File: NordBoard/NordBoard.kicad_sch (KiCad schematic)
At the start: 0 parts

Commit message: feat: readme & begin project
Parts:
- added SW1: SW_Push, symbol Switch:SW_Push
- added U1: MOUDLE-SEEEDUINO-XIAO, symbol XIAO_RP2040:MOUDLE-SEEEDUINO-XIAO
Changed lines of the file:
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@@
 	(generator_version "9.0")
 	(paper "A4")
+	(symbol
+		(lib_id "XIAO_RP2040:MOUDLE-SEEEDUINO-XIAO")
+		(at 58.42 48.26 0)
+		(unit 1)
+		(exclude_from_sim no)
+		(in_bom yes)
+		(on_board yes)
+		(dnp no)
+		(fields_autoplaced yes)
+		(property "Reference" "U1"
+			(at 59.69 33.02 0)
+			(effects
+				(font
+					(size 1.27 1.27)
+				)
+			)
+		)
+		(property "Value" "MOUDLE-SEEEDUINO-XIAO"
+			(at 59.69 35.56 0)
+			(effects
+				(font
+					(size 1.27 1.27)
+				)
+			)
+		)
+		(property "Footprint" ""
+			(at 41.91 45.72 0)
+			(effects
+				(font
+					(size 1.27 1.27)
+				)
+				(hide yes)
+			)
+		)
+		(property "Datasheet" ""
+			(at 41.91 45.72 0)
+			(effects
+				(font
+					(size 1.27 1.27)
+				)
+				(hide yes)
+			)
+		)
+		(property "Description" ""
+			(at 58.42 48.26 0)
+			(effects
+				(font
+					(size 1.27 1.27)
+				)
+				(hide yes)
+			)
+		)
+		(pin "13"
+		)
+		(pin "9"
+		)
+		(pin "1"
+		)
+		(pin "11"
+		)
+		(pin "12"
+		)
+		(pin "5"
+		)
+		(pin "3"
+		)
+		(pin "6"
+		)
+		(pin "14"
+		)
+		(pin "4"
+		)
+		(pin "2"
+		)
+		(pin "8"
+		)
+		(pin "10"
+		)
+		(pin "7"
+		)
+		(instances
+			(project ""
+				(path "/7cf7f72d-7ab1-4807-b592-339093d5ca44"
+					(reference "U1")
+					(unit 1)
+				)
+			)
+		)
+	)
+	(symbol
+		(lib_id "Switch:SW_Push")
+		(at 111.76 52.07 0)
+		(unit 1)
+		(exclude_from_sim no)
+		(in_bom yes)
+		(on_board yes)
+		(dnp no)
+		(fields_autoplaced yes)
+		(property "Reference" "SW1"
+			(at 111.76 44.45 0)
+			(effects
+				(font
+					(size 1.27 1.27)
+				)
+			)
+		)
+		(property "Value" "SW_Push"
+			(at 111.76 46.99 0)
+			(effects
+				(font
+					(size 1.27 1.27)
+				)
+			)
+		)
+		(property "Footprint" ""
+			(at 111.76 46.99 0)
+			(effects
+				(font
+					(size 1.27 1.27)
+				)
+				(hide yes)
+			)
+		)
+		(property "Datasheet" "~"
+			(at 111.76 46.99 0)
+			(effects
+				(font
+					(size 1.27 1.27)
+				)
+				(hide yes)
+			)
+		)
+		(property "Description" "Push button switch, generic, two pins"
+			(at 111.76 52.07 0)
+			(effects
+				(font
+					(size 1.27 1.27)
+				)
+				(hide yes)
+			)
+		)
+		(pin "1"
+		)
+		(pin "2"
+		)
+		(instances
+			(project ""
+				(path "/7cf7f72d-7ab1-4807-b592-339093d5ca44"
+					(reference "SW1")
+					(unit 1)
+				)
+			)
+		)
+	)
 	(sheet_instances
 		(path "/"

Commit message: sync
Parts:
- added SW10, SW11, SW12, SW13, SW14, SW16, SW17, SW18, SW19, SW2, SW20, SW21, SW3, SW4, SW5, SW6, SW7, SW8, SW9: SW_Push, PCM_Switch_Keyboard_Hotswap_Kailh:SW_Hotswap_Kailh_Choc_V1V2, symbol Switch:SW_Push
- SW1: footprint (none) -> PCM_Switch_Keyboard_Hotswap_Kailh:SW_Hotswap_Kailh_Choc_V1V2
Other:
- moved on the sheet: SW1, U1

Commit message: feat: PCB
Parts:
- SW1, SW10, SW11, SW12, SW13, SW14, SW16, SW17, SW18, SW19, SW2, SW20, SW21, SW3, SW4, SW5, SW6, SW7, SW8, SW9: footprint PCM_Switch_Keyboard_Hotswap_Kailh:SW_Hotswap_Kailh_Choc_V1V2 -> PCM_marbastlib-choc:SW_choc_v1_1u
- U1: footprint (none) -> Seeed Studio XIAO Series Library:XIAO-RP2040-DIP
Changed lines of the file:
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@@
 			)
 		)
-		(property "Footprint" "PCM_Switch_Keyboard_Hotswap_Kailh:SW_Hotswap_Kailh_Choc_V1V2"
+		(property "Footprint" "PCM_marbastlib-choc:SW_choc_v1_1u"
 			(at 161.29 62.23 0)
 			(effects
@@
 			)
 		)
-		(property "Footprint" "PCM_Switch_Keyboard_Hotswap_Kailh:SW_Hotswap_Kailh_Choc_V1V2"
+		(property "Footprint" "PCM_marbastlib-choc:SW_choc_v1_1u"
 			(at 92.71 59.69 0)
 			(effects
@@
 			)
 		)
-		(property "Footprint" "PCM_Switch_Keyboard_Hotswap_Kailh:SW_Hotswap_Kailh_Choc_V1V2"
+		(property "Footprint" "PCM_marbastlib-choc:SW_choc_v1_1u"
 			(at 46.99 60.96 0)
 			(effects
@@
 			)
 		)
-		(property "Footprint" "PCM_Switch_Keyboard_Hotswap_Kailh:SW_Hotswap_Kailh_Choc_V1V2"
+		(property "Footprint" "PCM_marbastlib-choc:SW_choc_v1_1u"
 			(at 115.57 54.61 0)
 			(effects
@@
 			)
 		)
-		(property "Footprint" ""
+		(property "Footprint" "Seeed Studio XIAO Series Library:XIAO-RP2040-DIP"
 			(at 213.36 46.99 0)
 			(effects
@@
 			)
 		)
-		(property "Footprint" "PCM_Switch_Keyboard_Hotswap_Kailh:SW_Hotswap_Kailh_Choc_V1V2"
+		(property "Footprint" "PCM_marbastlib-choc:SW_choc_v1_1u"
 			(at 161.29 36.83 0)
 			(effects
@@
 			)
 		)
-		(property "Footprint" "PCM_Switch_Keyboard_Hotswap_Kailh:SW_Hotswap_Kailh_Choc_V1V2"
+		(property "Footprint" "PCM_marbastlib-choc:SW_choc_v1_1u"
 			(at 115.57 29.21 0)
 			(effects
@@
 			)
 		)
-		(property "Footprint" "PCM_Switch_Keyboard_Hotswap_Kailh:SW_Hotswap_Kailh_Choc_V1V2"
+		(property "Footprint" "PCM_marbastlib-choc:SW_choc_v1_1u"
 			(at 161.29 49.53 0)
 			(effects
@@
 			)
 		)
-		(property "Footprint" "PCM_Switch_Keyboard_Hotswap_Kailh:SW_Hotswap_Kailh_Choc_V1V2"
+		(property "Footprint" "PCM_marbastlib-choc:SW_choc_v1_1u"
 			(at 69.85 39.37 0)
 			(effects
@@
 			)
 		)
-		(property "Footprint" "PCM_Switch_Keyboard_Hotswap_Kailh:SW_Hotswap_Kailh_Choc_V1V2"
+		(property "Footprint" "PCM_marbastlib-choc:SW_choc_v1_1u"
 			(at 92.71 34.29 0)
 			(effects
@@
 			)
 		)
-		(property "Footprint" "PCM_Switch_Keyboard_Hotswap_Kailh:SW_Hotswap_Kailh_Choc_V1V2"
+		(property "Footprint" "PCM_marbastlib-choc:SW_choc_v1_1u"
 			(at 69.85 64.77 0)
 			(effects
@@
 			)
 		)
-		(property "Footprint" "PCM_Switch_Keyboard_Hotswap_Kailh:SW_Hotswap_Kailh_Choc_V1V2"
+		(property "Footprint" "PCM_marbastlib-choc:SW_choc_v1_1u"
 			(at 184.15 64.77 0)
 			(effects
@@
 			)
 		)
-		(property "Footprint" "PCM_Switch_Keyboard_Hotswap_Kailh:SW_Hotswap_Kailh_Choc_V1V2"
+		(property "Footprint" "PCM_marbastlib-choc:SW_choc_v1_1u"
 			(at 92.71 46.99 0)
 			(effects
@@
 			)
 		)
-		(property "Footprint" "PCM_Switch_Keyboard_Hotswap_Kailh:SW_Hotswap_Kailh_Choc_V1V2"
+		(property "Footprint" "PCM_marbastlib-choc:SW_choc_v1_1u"
 			(at 138.43 33.02 0)
 			(effects
@@
 			)
 		)
-		(property "Footprint" "PCM_Switch_Keyboard_Hotswap_Kailh:SW_Hotswap_Kailh_Choc_V1V2"
+		(property "Footprint" "PCM_marbastlib-choc:SW_choc_v1_1u"
 			(at 138.43 58.42 0)
 			(effects
@@
 			)
 		)
-		(property "Footprint" "PCM_Switch_Keyboard_Hotswap_Kailh:SW_Hotswap_Kailh_Choc_V1V2"
+		(property "Footprint" "PCM_marbastlib-choc:SW_choc_v1_1u"
 			(at 184.15 39.37 0)
 			(effects
@@
 			)
 		)
-		(property "Footprint" "PCM_Switch_Keyboard_Hotswap_Kailh:SW_Hotswap_Kailh_Choc_V1V2"
+		(property "Footprint" "PCM_marbastlib-choc:SW_choc_v1_1u"
 			(at 184.15 52.07 0)
 			(effects
@@
 			)
 		)
-		(property "Footprint" "PCM_Switch_Keyboard_Hotswap_Kailh:SW_Hotswap_Kailh_Choc_V1V2"
+		(property "Footprint" "PCM_marbastlib-choc:SW_choc_v1_1u"
 			(at 46.99 48.26 0)
 			(effects
@@
 			)
 		)
-		(property "Footprint" "PCM_Switch_Keyboard_Hotswap_Kailh:SW_Hotswap_Kailh_Choc_V1V2"
+		(property "Footprint" "PCM_marbastlib-choc:SW_choc_v1_1u"
 			(at 115.57 41.91 0)
 			(effects
@@
 			)
 		)
-		(property "Footprint" "PCM_Switch_Keyboard_Hotswap_Kailh:SW_Hotswap_Kailh_Choc_V1V2"
+		(property "Footprint" "PCM_marbastlib-choc:SW_choc_v1_1u"
 			(at 138.43 45.72 0)
 			(effects
@@
 			)
 		)
-		(property "Footprint" "PCM_Switch_Keyboard_Hotswap_Kailh:SW_Hotswap_Kailh_Choc_V1V2"
+		(property "Footprint" "PCM_marbastlib-choc:SW_choc_v1_1u"
 			(at 69.85 52.07 0)
 			(effects

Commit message: feat: work on schem layout
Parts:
- removed SW16, SW2, SW9: SW_Push, PCM_marbastlib-choc:SW_choc_v1_1u, symbol Switch:SW_Push
- added D10, D11, D12, D13, D14, D15, D16, D17, D18, D2, D3, D4, D5, D6, D7, D8, D9: D, symbol Device:D
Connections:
- net Col3: now reaches SW20.1
- net Col3: now also SW13.1, SW7.1, U1.5 (PA8_A4_D4_SDA)
- net at SW20.2: now also D13.2 (A)
- net Col0: now reaches SW17.1
- net Col0: now also SW10.1, SW3.1, U1.2 (PA4_A1_D1)
- net at SW17.2: now also D4.2 (A)
- net at SW4.2: now also D17.2 (A)
- net Col1: now reaches SW18.1
- net Col1: now also SW11.1, SW5.1, U1.3 (PA10_A2_D2)
- net at SW18.2: now also D7.2 (A)
- net Row1: now reaches U1.10 (PA5_A9_D9_MISO)
- net Row1: now also D12.1 (K), D15.1 (K), D3.1 (K), D6.1 (K), D9.1 (K)
- net Row0: now reaches U1.11 (PA6_A10_D10_MOSI)
- net Row0: now also D11.1 (K), D14.1 (K), D2.1 (K), D5.1 (K), D8.1 (K)
- net GND: now reaches U1.13 (GND)
- net Col2: now reaches U1.4 (PA11_A3_D3)
- net Col2: now also SW12.1, SW19.1, SW6.1
- net Row2: now reaches U1.9 (PA7_A8_D8_SCK)
- net Row2: now also D10.1 (K), D13.1 (K), D16.1 (K), D4.1 (K), D7.1 (K)
- net at SW7.2: now also D11.2 (A)
- net at SW5.2: now also D5.2 (A)
- net at SW13.2: now also D12.2 (A)
- net at SW3.2: now also D2.2 (A)
- net Col4: now reaches SW21.1
- net Col4: now also SW14.1, SW8.1
- net at SW21.2: now also D16.2 (A)
- net at SW10.2: now also D3.2 (A)
- net at SW6.2: now also D8.2 (A)
- net at SW19.2: now also D10.2 (A)
- net at SW8.2: now also D14.2 (A)
- net at SW14.2: now also D15.2 (A)
- net at SW1.2: now also D18.2 (A)
- net at SW11.2: now also D6.2 (A)
- net at SW12.2: now also D9.2 (A)
- new net Row3: D17.1 (K), D18.1 (K)
- no-connect marks 0 -> 4
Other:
- moved on the sheet: SW1, SW10, SW11, SW12, SW17, SW18, SW19, SW3, SW4, SW5, SW6, U1

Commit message: feat: schem
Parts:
- removed D10, D11, D12, D13, D14, D15, D16, D17, D18, D2, D3, D4, D5, D6, D7, D8, D9: D, symbol Device:D
- removed SW1, SW10, SW11, SW12, SW13, SW14, SW17, SW18, SW19, SW20, SW21, SW3, SW4, SW5, SW6, SW7, SW8: SW_Push, PCM_marbastlib-choc:SW_choc_v1_1u, symbol Switch:SW_Push
- removed U1: MOUDLE-SEEEDUINO-XIAO, Seeed Studio XIAO Series Library:XIAO-RP2040-DIP, symbol XIAO_RP2040:MOUDLE-SEEEDUINO-XIAO
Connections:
- no-connect marks 4 -> 0
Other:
- added sheet left (side.kicad_sch)
- added sheet right (right.kicad_sch)

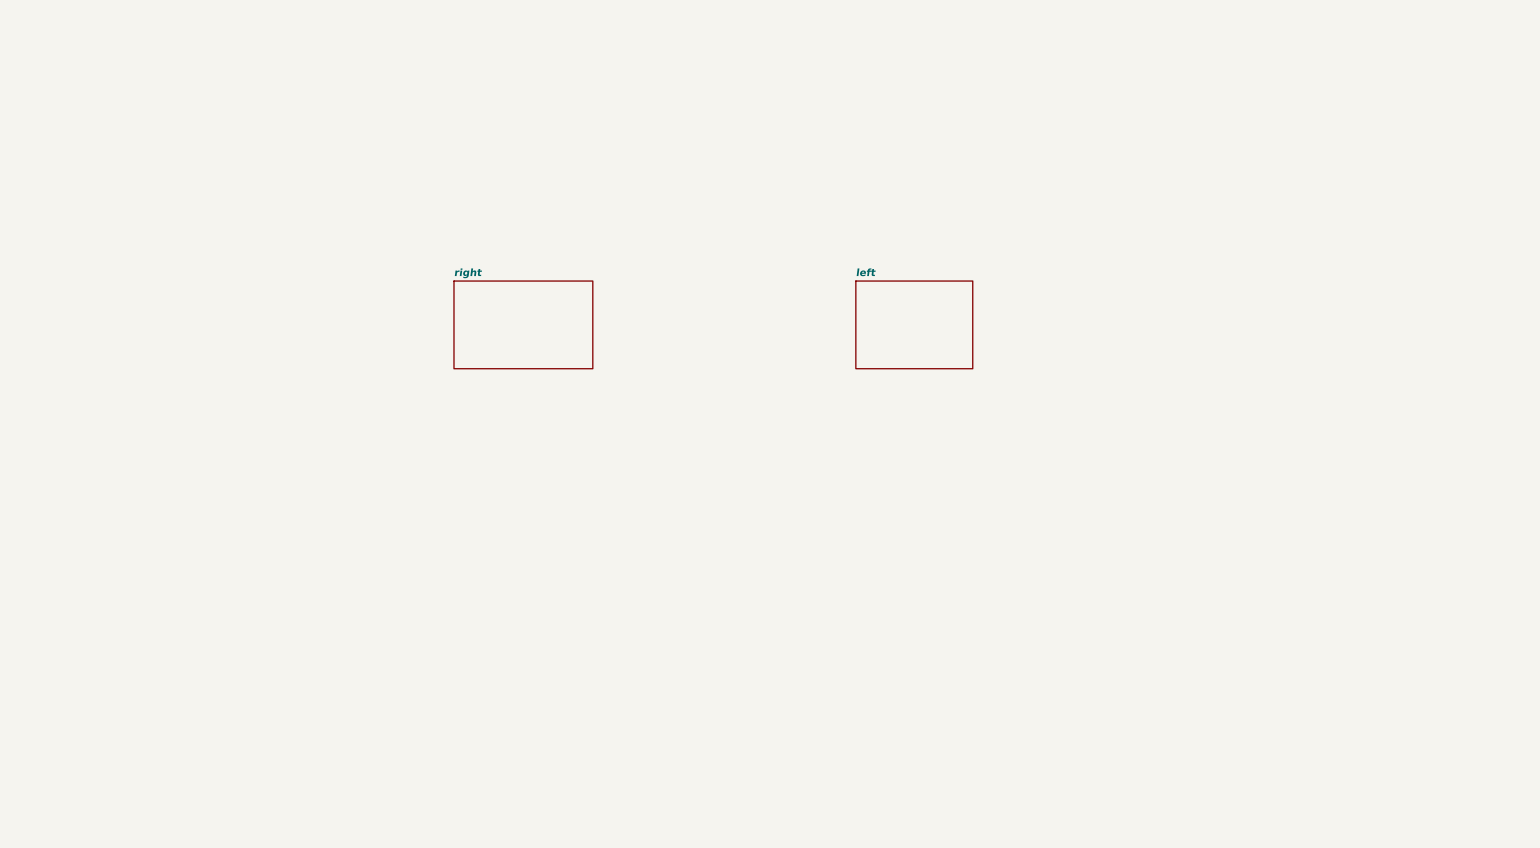
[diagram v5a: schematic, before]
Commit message: feat: finish pcb layout and cleanup todo routing
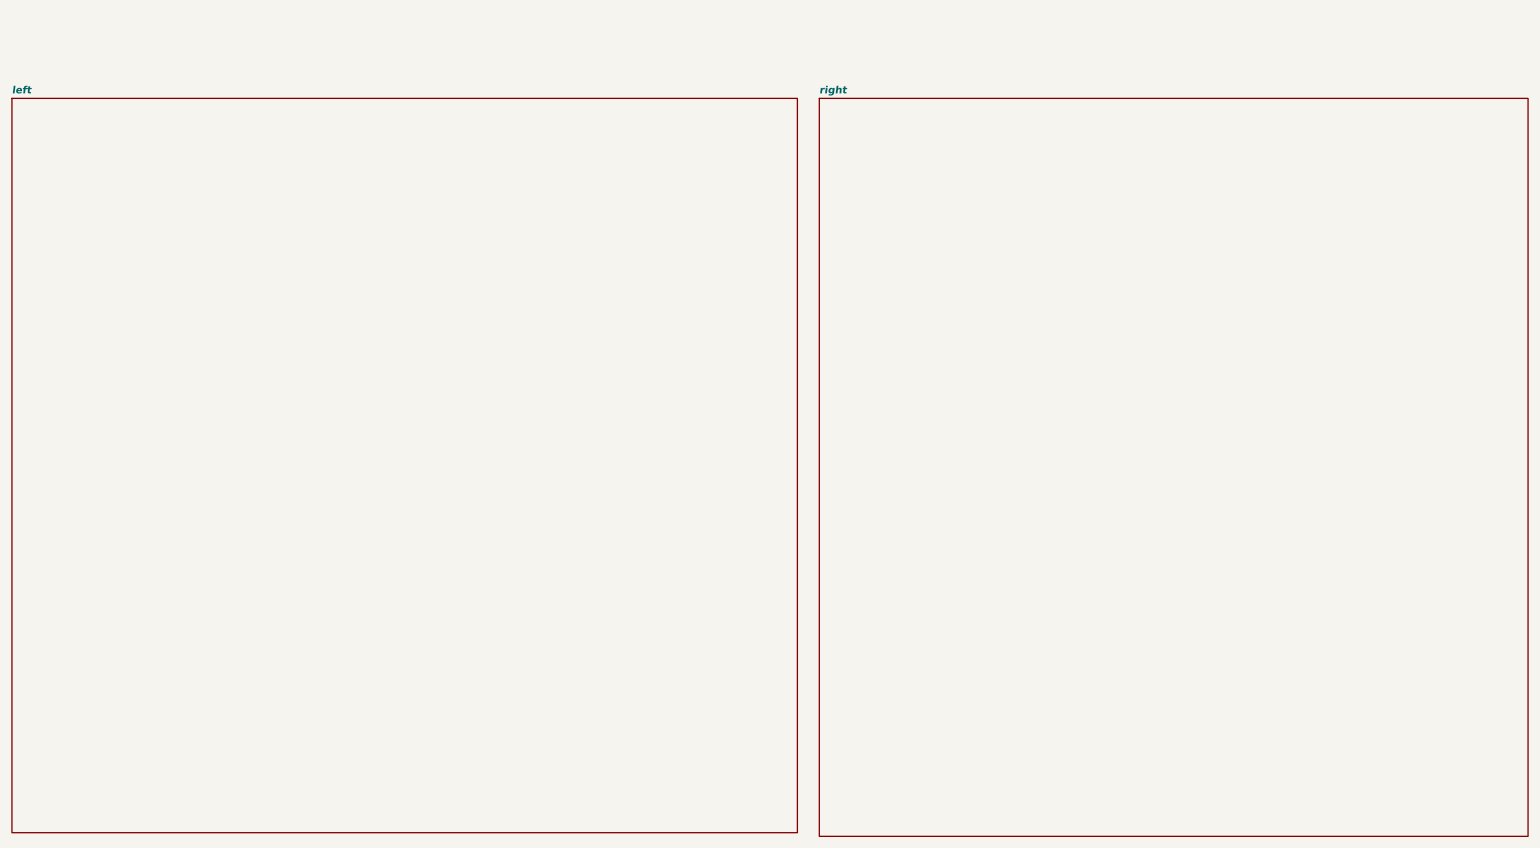
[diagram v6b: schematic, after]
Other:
- sheet right: file right.kicad_sch -> side.kicad_sch
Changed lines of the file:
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@@
 	(paper "A4")
 	(sheet
-		(at 162.56 60.96)
-		(size 20.32 15.24)
+		(at 15.875 29.21)
+		(size 136.525 127.635)
 		(exclude_from_sim no)
 		(in_bom yes)
@@
 		)
 		(property "Sheetname" "left"
-			(at 162.56 60.2484 0)
+			(at 15.875 28.4984 0)
 			(effects
 				(font
@@
 		)
 		(property "Sheetfile" "side.kicad_sch"
-			(at 162.56 76.7846 0)
+			(at 15.875 157.4296 0)
 			(effects
 				(font
@@
 	)
 	(sheet
-		(at 92.71 60.96)
-		(size 24.13 15.24)
+		(at 156.21 29.21)
+		(size 123.19 128.27)
 		(exclude_from_sim no)
 		(in_bom yes)
@@
 		)
 		(property "Sheetname" "right"
-			(at 92.71 60.2484 0)
+			(at 156.21 28.4984 0)
 			(effects
 				(font
@@
 			)
 		)
-		(property "Sheetfile" "right.kicad_sch"
-			(at 92.71 76.7846 0)
+		(property "Sheetfile" "side.kicad_sch"
+			(at 156.21 158.0646 0)
 			(effects
 				(font
